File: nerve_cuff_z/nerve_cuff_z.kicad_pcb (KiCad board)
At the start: 2 copper layers, 4 x 5.7 mm, 4 parts

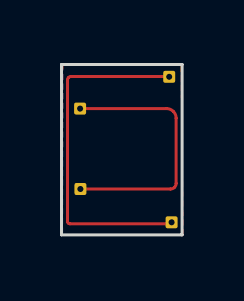
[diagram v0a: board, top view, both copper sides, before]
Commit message: fixing minor DRC problems for z cuff
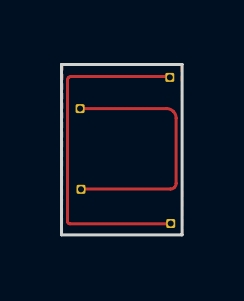
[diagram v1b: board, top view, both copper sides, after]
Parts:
- removed the REF** at (103.5, 65.3)
- removed the REF** at (100.6, 69.1)
- removed the REF** at (103.6, 70.2)
- added REF**: solder_wire_pad, nerve_cuff_pad:solder_wire_pad, F.Cu at (103.6, 70.2)
- added REF**: solder_wire_pad, nerve_cuff_pad:solder_wire_pad, F.Cu at (103.6, 65.3)
- added REF**: solder_wire_pad, nerve_cuff_pad:solder_wire_pad, F.Cu at (100.6, 69.1)
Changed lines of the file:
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@@
   (net 0 "")
   (footprint "nerve_cuff_pad:solder_wire_pad" (layer "F.Cu")
-    (at 103.55 65.33)
+    (at 103.6 70.22)
     (descr "Soldered wire connection, for a single 0.1 mm² wire, basic insulation, conductor diameter 0.4mm, outer diameter 1mm, size source Multi-Contact FLEXI-E 0.1 (https://ec.staubli.com/AcroFiles/Catalogues/TM_Cab-Main-11014119_(en)_hi.pdf), bend radius 3 times outer diameter, generated with kicad-footprint-generator")
     (tags "connector wire 0.1sqmm")
@@
     (fp_line (start 0.2 0.2) (end 0.2 -0.2)
       (stroke (width 0.05) (type solid)) (layer "F.CrtYd"))
-    (pad "1" thru_hole roundrect (at 0 0) (size 0.4 0.4) (drill 0.2) (layers "*.Cu" "*.Mask") (roundrect_rratio 0.15625))
+    (pad "1" thru_hole roundrect (at 0 0) (size 0.3 0.3) (drill 0.2) (layers "*.Cu" "*.Mask") (roundrect_rratio 0.15625))
     (model "${KICAD6_3DMODEL_DIR}/Connector_Wire.3dshapes/SolderWire-0.1sqmm_1x01_D0.4mm_OD1mm.wrl"
       (offset (xyz 0 0 0))
@@
   )
   (footprint "nerve_cuff_pad:solder_wire_pad" (layer "F.Cu")
-    (at 100.59 69.07)
+    (at 103.57 65.35)
     (descr "Soldered wire connection, for a single 0.1 mm² wire, basic insulation, conductor diameter 0.4mm, outer diameter 1mm, size source Multi-Contact FLEXI-E 0.1 (https://ec.staubli.com/AcroFiles/Catalogues/TM_Cab-Main-11014119_(en)_hi.pdf), bend radius 3 times outer diameter, generated with kicad-footprint-generator")
     (tags "connector wire 0.1sqmm")
@@
     (fp_line (start 0.2 0.2) (end 0.2 -0.2)
       (stroke (width 0.05) (type solid)) (layer "F.CrtYd"))
-    (pad "1" thru_hole roundrect (at 0 0) (size 0.4 0.4) (drill 0.2) (layers "*.Cu" "*.Mask") (roundrect_rratio 0.15625))
+    (pad "1" thru_hole roundrect (at 0 0) (size 0.3 0.3) (drill 0.2) (layers "*.Cu" "*.Mask") (roundrect_rratio 0.15625))
     (model "${KICAD6_3DMODEL_DIR}/Connector_Wire.3dshapes/SolderWire-0.1sqmm_1x01_D0.4mm_OD1mm.wrl"
       (offset (xyz 0 0 0))
@@
     (fp_line (start 0.2 0.2) (end 0.2 -0.2)
       (stroke (width 0.05) (type solid)) (layer "F.CrtYd"))
-    (pad "1" thru_hole roundrect (at 0 0) (size 0.4 0.4) (drill 0.2) (layers "*.Cu" "*.Mask") (roundrect_rratio 0.15625))
+    (pad "1" thru_hole roundrect (at 0 0) (size 0.3 0.3) (drill 0.2) (layers "*.Cu" "*.Mask") (roundrect_rratio 0.15625))
     (model "${KICAD6_3DMODEL_DIR}/Connector_Wire.3dshapes/SolderWire-0.1sqmm_1x01_D0.4mm_OD1mm.wrl"
       (offset (xyz 0 0 0))
@@
   )
   (footprint "nerve_cuff_pad:solder_wire_pad" (layer "F.Cu")
-    (at 103.63 70.18)
+    (at 100.61 69.08)
     (descr "Soldered wire connection, for a single 0.1 mm² wire, basic insulation, conductor diameter 0.4mm, outer diameter 1mm, size source Multi-Contact FLEXI-E 0.1 (https://ec.staubli.com/AcroFiles/Catalogues/TM_Cab-Main-11014119_(en)_hi.pdf), bend radius 3 times outer diameter, generated with kicad-footprint-generator")
     (tags "connector wire 0.1sqmm")
@@
     (fp_line (start 0.2 0.2) (end 0.2 -0.2)
       (stroke (width 0.05) (type solid)) (layer "F.CrtYd"))
-    (pad "1" thru_hole roundrect (at 0 0) (size 0.4 0.4) (drill 0.2) (layers "*.Cu" "*.Mask") (roundrect_rratio 0.15625))
+    (pad "1" thru_hole roundrect (at 0 0) (size 0.3 0.3) (drill 0.2) (layers "*.Cu" "*.Mask") (roundrect_rratio 0.15625))
     (model "${KICAD6_3DMODEL_DIR}/Connector_Wire.3dshapes/SolderWire-0.1sqmm_1x01_D0.4mm_OD1mm.wrl"
       (offset (xyz 0 0 0))
@@
   (segment (start 100.16 65.439497) (end 100.16 70.144644) (width 0.1) (layer "F.Cu") (net 0))
   (segment (start 103.54 65.32) (end 100.279497 65.32) (width 0.1) (layer "F.Cu") (net 0))
+  (segment (start 103.592218 69.07) (end 100.59 69.07) (width 0.1) (layer "F.Cu") (net 0))
   (segment (start 103.461706 66.39) (end 100.58 66.39) (width 0.1) (layer "F.Cu") (net 0))
-  (segment (start 103.592218 69.07) (end 100.59 69.07) (width 0.1) (layer "F.Cu") (net 0))
   (segment (start 103.58 70.23) (end 103.63 70.18) (width 0.1) (layer "F.Cu") (net 0))
   (arc (start 100.279497 65.32) (mid 100.233768 65.329096) (end 100.195 65.355) (width 0.1) (layer "F.Cu") (net 0))

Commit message: all boards cleaned up + passing DRC
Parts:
- moved REF** 0.07 mm to (103.5, 70.2)
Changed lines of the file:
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@@
   (net 0 "")
   (footprint "nerve_cuff_pad:solder_wire_pad" (layer "F.Cu")
-    (at 103.6 70.22)
+    (at 103.53 70.21)
     (descr "Soldered wire connection, for a single 0.1 mm² wire, basic insulation, conductor diameter 0.4mm, outer diameter 1mm, size source Multi-Contact FLEXI-E 0.1 (https://ec.staubli.com/AcroFiles/Catalogues/TM_Cab-Main-11014119_(en)_hi.pdf), bend radius 3 times outer diameter, generated with kicad-footprint-generator")
     (tags "connector wire 0.1sqmm")
@@
         (effects (font (size 1 1) (thickness 0.15)))
     )
-    (fp_line (start -0.2 -0.2) (end -0.2 0.2)
+    (fp_line (start -0.3 -0.3) (end -0.3 0.3)
       (stroke (width 0.05) (type solid)) (layer "F.CrtYd"))
-    (fp_line (start -0.2 0.2) (end 0.2 0.2)
+    (fp_line (start -0.3 0.3) (end 0.3 0.3)
       (stroke (width 0.05) (type solid)) (layer "F.CrtYd"))
-    (fp_line (start 0.2 -0.2) (end -0.2 -0.2)
+    (fp_line (start 0.3 -0.3) (end -0.3 -0.3)
       (stroke (width 0.05) (type solid)) (layer "F.CrtYd"))
-    (fp_line (start 0.2 0.2) (end 0.2 -0.2)
+    (fp_line (start 0.3 0.3) (end 0.3 -0.3)
       (stroke (width 0.05) (type solid)) (layer "F.CrtYd"))
     (pad "1" thru_hole roundrect (at 0 0) (size 0.3 0.3) (drill 0.2) (layers "*.Cu" "*.Mask") (roundrect_rratio 0.15625))
@@
         (effects (font (size 1 1) (thickness 0.15)))
     )
-    (fp_line (start -0.2 -0.2) (end -0.2 0.2)
+    (fp_line (start -0.3 -0.3) (end -0.3 0.3)
       (stroke (width 0.05) (type solid)) (layer "F.CrtYd"))
-    (fp_line (start -0.2 0.2) (end 0.2 0.2)
+    (fp_line (start -0.3 0.3) (end 0.3 0.3)
       (stroke (width 0.05) (type solid)) (layer "F.CrtYd"))
-    (fp_line (start 0.2 -0.2) (end -0.2 -0.2)
+    (fp_line (start 0.3 -0.3) (end -0.3 -0.3)
       (stroke (width 0.05) (type solid)) (layer "F.CrtYd"))
-    (fp_line (start 0.2 0.2) (end 0.2 -0.2)
+    (fp_line (start 0.3 0.3) (end 0.3 -0.3)
       (stroke (width 0.05) (type solid)) (layer "F.CrtYd"))
     (pad "1" thru_hole roundrect (at 0 0) (size 0.3 0.3) (drill 0.2) (layers "*.Cu" "*.Mask") (roundrect_rratio 0.15625))
@@
         (effects (font (size 1 1) (thickness 0.15)))
     )
-    (fp_line (start -0.2 -0.2) (end -0.2 0.2)
+    (fp_line (start -0.3 -0.3) (end -0.3 0.3)
       (stroke (width 0.05) (type solid)) (layer "F.CrtYd"))
-    (fp_line (start -0.2 0.2) (end 0.2 0.2)
+    (fp_line (start -0.3 0.3) (end 0.3 0.3)
       (stroke (width 0.05) (type solid)) (layer "F.CrtYd"))
-    (fp_line (start 0.2 -0.2) (end -0.2 -0.2)
+    (fp_line (start 0.3 -0.3) (end -0.3 -0.3)
       (stroke (width 0.05) (type solid)) (layer "F.CrtYd"))
-    (fp_line (start 0.2 0.2) (end 0.2 -0.2)
+    (fp_line (start 0.3 0.3) (end 0.3 -0.3)
       (stroke (width 0.05) (type solid)) (layer "F.CrtYd"))
     (pad "1" thru_hole roundrect (at 0 0) (size 0.3 0.3) (drill 0.2) (layers "*.Cu" "*.Mask") (roundrect_rratio 0.15625))
@@
         (effects (font (size 1 1) (thickness 0.15)))
     )
-    (fp_line (start -0.2 -0.2) (end -0.2 0.2)
+    (fp_line (start -0.3 -0.3) (end -0.3 0.3)
       (stroke (width 0.05) (type solid)) (layer "F.CrtYd"))
-    (fp_line (start -0.2 0.2) (end 0.2 0.2)
+    (fp_line (start -0.3 0.3) (end 0.3 0.3)
       (stroke (width 0.05) (type solid)) (layer "F.CrtYd"))
-    (fp_line (start 0.2 -0.2) (end -0.2 -0.2)
+    (fp_line (start 0.3 -0.3) (end -0.3 -0.3)
       (stroke (width 0.05) (type solid)) (layer "F.CrtYd"))
-    (fp_line (start 0.2 0.2) (end 0.2 -0.2)
+    (fp_line (start 0.3 0.3) (end 0.3 -0.3)
       (stroke (width 0.05) (type solid)) (layer "F.CrtYd"))
     (pad "1" thru_hole roundrect (at 0 0) (size 0.3 0.3) (drill 0.2) (layers "*.Cu" "*.Mask") (roundrect_rratio 0.15625))
@@
   )
   (dimension (type aligned) (layer "F.SilkS")
-    (pts (xy 103.98 64.92) (xy 103.98 70.6))
+    (pts (xy 103.3 65.29) (xy 103.3 70.97))
     (height -5.97)
-    (gr_text "5.6800 mm" (at 108.8 67.76 90) (layer "F.SilkS")
+    (gr_text "5.6800 mm" (at 108.12 68.13 90) (layer "F.SilkS")
       (effects (font (size 1 1) (thickness 0.15)))
     )
@@
     (style (thickness 0.15) (arrow_length 1.27) (text_position_mode 0) (extension_height 0.58642) (extension_offset 0.5) keep_text_aligned)
   )
-  (segment (start 100.245355 70.23) (end 103.58 70.23) (width 0.1) (layer "F.Cu") (net 0))
+  (segment (start 100.245355 70.23) (end 103.51 70.23) (width 0.1) (layer "F.Cu") (net 0))
   (segment (start 103.78 68.882218) (end 103.78 66.708293) (width 0.1) (layer "F.Cu") (net 0))
+  (segment (start 103.54 65.32) (end 100.279497 65.32) (width 0.1) (layer "F.Cu") (net 0))
   (segment (start 100.16 65.439497) (end 100.16 70.144644) (width 0.1) (layer "F.Cu") (net 0))
-  (segment (start 103.54 65.32) (end 100.279497 65.32) (width 0.1) (layer "F.Cu") (net 0))
   (segment (start 103.592218 69.07) (end 100.59 69.07) (width 0.1) (layer "F.Cu") (net 0))
   (segment (start 103.461706 66.39) (end 100.58 66.39) (width 0.1) (layer "F.Cu") (net 0))
-  (segment (start 103.58 70.23) (end 103.63 70.18) (width 0.1) (layer "F.Cu") (net 0))
-  (arc (start 100.279497 65.32) (mid 100.233768 65.329096) (end 100.195 65.355) (width 0.1) (layer "F.Cu") (net 0))
   (arc (start 103.78 68.882218) (mid 103.765705 68.954079) (end 103.725 69.015) (width 0.1) (layer "F.Cu") (net 0))
+  (arc (start 100.195 65.355) (mid 100.169096 65.393767) (end 100.16 65.439497) (width 0.1) (layer "F.Cu") (net 0))
+  (arc (start 100.185 70.205) (mid 100.212691 70.223508) (end 100.245355 70.23) (width 0.1) (layer "F.Cu") (net 0))
   (arc (start 103.686774 66.483226) (mid 103.583512 66.414228) (end 103.461706 66.39) (width 0.1) (layer "F.Cu") (net 0))
   (arc (start 103.725 69.015) (mid 103.664079 69.055705) (end 103.592218 69.07) (width 0.1) (layer "F.Cu") (net 0))
   (arc (start 103.686774 66.483226) (mid 103.755771 66.586487) (end 103.78 66.708293) (width 0.1) (layer "F.Cu") (net 0))
   (arc (start 100.16 70.144644) (mid 100.166497 70.177308) (end 100.185 70.205) (width 0.1) (layer "F.Cu") (net 0))
-  (arc (start 100.185 70.205) (mid 100.212691 70.223496) (end 100.245355 70.23) (width 0.1) (layer "F.Cu") (net 0))
-  (arc (start 100.195 65.355) (mid 100.169096 65.393767) (end 100.16 65.439497) (width 0.1) (layer "F.Cu") (net 0))
+  (arc (start 100.279497 65.32) (mid 100.233768 65.329096) (end 100.195 65.355) (width 0.1) (layer "F.Cu") (net 0))
   (zone (net 0) (net_name "") (layer "F.Cu") (hatch edge 0.1)
     (connect_pads (clearance 0.05))

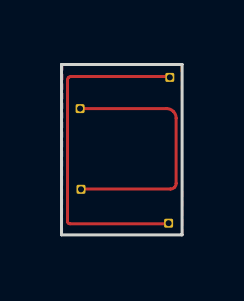
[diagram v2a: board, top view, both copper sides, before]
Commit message: updating clearances for xy gradient board
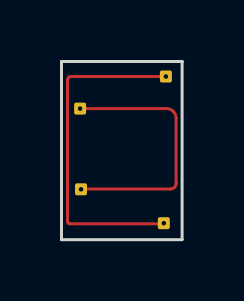
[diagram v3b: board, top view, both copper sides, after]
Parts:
- moved REF** 0.16 mm to (103.4, 70.2)
- moved REF** 0.13 mm to (103.4, 65.3)
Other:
- board size 4 x 5.7 mm -> 4 x 5.9 mm
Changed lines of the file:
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@@
   (net 0 "")
   (footprint "nerve_cuff_pad:solder_wire_pad" (layer "F.Cu")
-    (at 103.53 70.21)
+    (at 103.37 70.21)
     (descr "Soldered wire connection, for a single 0.1 mm² wire, basic insulation, conductor diameter 0.4mm, outer diameter 1mm, size source Multi-Contact FLEXI-E 0.1 (https://ec.staubli.com/AcroFiles/Catalogues/TM_Cab-Main-11014119_(en)_hi.pdf), bend radius 3 times outer diameter, generated with kicad-footprint-generator")
     (tags "connector wire 0.1sqmm")
@@
     (fp_line (start 0.3 0.3) (end 0.3 -0.3)
       (stroke (width 0.05) (type solid)) (layer "F.CrtYd"))
-    (pad "1" thru_hole roundrect (at 0 0) (size 0.3 0.3) (drill 0.2) (layers "*.Cu" "*.Mask") (roundrect_rratio 0.15625))
+    (pad "1" thru_hole roundrect (at 0 0) (size 0.4 0.4) (drill 0.15) (layers "*.Cu" "*.Mask") (roundrect_rratio 0.15625))
     (model "${KICAD6_3DMODEL_DIR}/Connector_Wire.3dshapes/SolderWire-0.1sqmm_1x01_D0.4mm_OD1mm.wrl"
       (offset (xyz 0 0 0))
@@
   )
   (footprint "nerve_cuff_pad:solder_wire_pad" (layer "F.Cu")
-    (at 103.57 65.35)
+    (at 103.44 65.32)
     (descr "Soldered wire connection, for a single 0.1 mm² wire, basic insulation, conductor diameter 0.4mm, outer diameter 1mm, size source Multi-Contact FLEXI-E 0.1 (https://ec.staubli.com/AcroFiles/Catalogues/TM_Cab-Main-11014119_(en)_hi.pdf), bend radius 3 times outer diameter, generated with kicad-footprint-generator")
     (tags "connector wire 0.1sqmm")
@@
     (fp_line (start 0.3 0.3) (end 0.3 -0.3)
       (stroke (width 0.05) (type solid)) (layer "F.CrtYd"))
-    (pad "1" thru_hole roundrect (at 0 0) (size 0.3 0.3) (drill 0.2) (layers "*.Cu" "*.Mask") (roundrect_rratio 0.15625))
+    (pad "1" thru_hole roundrect (at 0 0) (size 0.4 0.4) (drill 0.15) (layers "*.Cu" "*.Mask") (roundrect_rratio 0.15625))
     (model "${KICAD6_3DMODEL_DIR}/Connector_Wire.3dshapes/SolderWire-0.1sqmm_1x01_D0.4mm_OD1mm.wrl"
       (offset (xyz 0 0 0))
@@
     (fp_line (start 0.3 0.3) (end 0.3 -0.3)
       (stroke (width 0.05) (type solid)) (layer "F.CrtYd"))
-    (pad "1" thru_hole roundrect (at 0 0) (size 0.3 0.3) (drill 0.2) (layers "*.Cu" "*.Mask") (roundrect_rratio 0.15625))
+    (pad "1" thru_hole roundrect (at 0 0) (size 0.4 0.4) (drill 0.15) (layers "*.Cu" "*.Mask") (roundrect_rratio 0.15625))
     (model "${KICAD6_3DMODEL_DIR}/Connector_Wire.3dshapes/SolderWire-0.1sqmm_1x01_D0.4mm_OD1mm.wrl"
       (offset (xyz 0 0 0))
@@
     (fp_line (start 0.3 0.3) (end 0.3 -0.3)
       (stroke (width 0.05) (type solid)) (layer "F.CrtYd"))
-    (pad "1" thru_hole roundrect (at 0 0) (size 0.3 0.3) (drill 0.2) (layers "*.Cu" "*.Mask") (roundrect_rratio 0.15625))
+    (pad "1" thru_hole roundrect (at 0 0) (size 0.4 0.4) (drill 0.15) (layers "*.Cu" "*.Mask") (roundrect_rratio 0.15625))
     (model "${KICAD6_3DMODEL_DIR}/Connector_Wire.3dshapes/SolderWire-0.1sqmm_1x01_D0.4mm_OD1mm.wrl"
       (offset (xyz 0 0 0))
@@
     )
   )
-  (gr_line (start 103.98 70.6) (end 103.98 64.92)
+  (gr_line (start 103.98 70.76) (end 103.98 64.82)
     (stroke (width 0.1) (type default)) (layer "Edge.Cuts"))
-  (gr_line (start 103.98 64.92) (end 99.96 64.92)
+  (gr_line (start 103.98 64.82) (end 99.96 64.82)
     (stroke (width 0.1) (type default)) (layer "Edge.Cuts"))
-  (gr_line (start 99.96 64.92) (end 99.96 70.6)
+  (gr_line (start 99.96 64.82) (end 99.96 70.76)
     (stroke (width 0.1) (type default)) (layer "Edge.Cuts"))
-  (gr_line (start 99.96 70.6) (end 103.98 70.6)
+  (gr_line (start 99.96 70.76) (end 103.98 70.76)
     (stroke (width 0.1) (type default)) (layer "Edge.Cuts"))
   (dimension (type aligned) (layer "F.SilkS")
@@
     (style (thickness 0.15) (arrow_length 1.27) (text_position_mode 0) (extension_height 0.58642) (extension_offset 0.5) keep_text_aligned)
   )
-  (dimension (type aligned) (layer "F.SilkS")
-    (pts (xy 103.3 65.29) (xy 103.3 70.97))
-    (height -5.97)
-    (gr_text "5.6800 mm" (at 108.12 68.13 90) (layer "F.SilkS")
+  (dimension (type aligned) (layer "Edge.Cuts")
+    (pts (xy 103.97 64.83) (xy 103.98 70.77))
+    (height -3.197611)
+    (gr_text "5.9400 mm" (at 108.322604 67.792681 270.0964575) (layer "Edge.Cuts")
       (effects (font (size 1 1) (thickness 0.15)))
     )
     (format (prefix "") (suffix "") (units 3) (units_format 1) (precision 4))
-    (style (thickness 0.15) (arrow_length 1.27) (text_position_mode 0) (extension_height 0.58642) (extension_offset 0.5) keep_text_aligned)
+    (style (thickness 0.1) (arrow_length 1.27) (text_position_mode 0) (extension_height 0.58642) (extension_offset 0.5) keep_text_aligned)
   )
   (segment (start 100.245355 70.23) (end 103.51 70.23) (width 0.1) (layer "F.Cu") (net 0))
+  (segment (start 100.256529 65.32) (end 100.255861 65.320668) (width 0.1) (layer "F.Cu") (net 0))
   (segment (start 103.78 68.882218) (end 103.78 66.708293) (width 0.1) (layer "F.Cu") (net 0))
-  (segment (start 103.54 65.32) (end 100.279497 65.32) (width 0.1) (layer "F.Cu") (net 0))
+  (segment (start 103.121336 65.32) (end 100.256529 65.32) (width 0.1) (layer "F.Cu") (net 0))
   (segment (start 100.16 65.439497) (end 100.16 70.144644) (width 0.1) (layer "F.Cu") (net 0))
   (segment (start 103.592218 69.07) (end 100.59 69.07) (width 0.1) (layer "F.Cu") (net 0))
+  (segment (start 103.121336 65.32) (end 103.44 65.32) (width 0.1) (layer "F.Cu") (net 0))
+  (segment (start 103.120668 65.320668) (end 103.121336 65.32) (width 0.1) (layer "F.Cu") (net 0))
   (segment (start 103.461706 66.39) (end 100.58 66.39) (width 0.1) (layer "F.Cu") (net 0))
   (arc (start 103.78 68.882218) (mid 103.765705 68.954079) (end 103.725 69.015) (width 0.1) (layer "F.Cu") (net 0))
+  (arc (start 103.686774 66.483226) (mid 103.583512 66.414228) (end 103.461706 66.39) (width 0.1) (layer "F.Cu") (net 0))
   (arc (start 100.195 65.355) (mid 100.169096 65.393767) (end 100.16 65.439497) (width 0.1) (layer "F.Cu") (net 0))
+  (arc (start 103.725 69.015) (mid 103.664079 69.055705) (end 103.592218 69.07) (width 0.1) (layer "F.Cu") (net 0))
+  (arc (start 100.16 70.144644) (mid 100.166497 70.177308) (end 100.185 70.205) (width 0.1) (layer "F.Cu") (net 0))
+  (arc (start 103.686774 66.483226) (mid 103.755771 66.586487) (end 103.78 66.708293) (width 0.1) (layer "F.Cu") (net 0))
   (arc (start 100.185 70.205) (mid 100.212691 70.223508) (end 100.245355 70.23) (width 0.1) (layer "F.Cu") (net 0))
-  (arc (start 103.686774 66.483226) (mid 103.583512 66.414228) (end 103.461706 66.39) (width 0.1) (layer "F.Cu") (net 0))
-  (arc (start 103.725 69.015) (mid 103.664079 69.055705) (end 103.592218 69.07) (width 0.1) (layer "F.Cu") (net 0))
-  (arc (start 103.686774 66.483226) (mid 103.755771 66.586487) (end 103.78 66.708293) (width 0.1) (layer "F.Cu") (net 0))
-  (arc (start 100.16 70.144644) (mid 100.166497 70.177308) (end 100.185 70.205) (width 0.1) (layer "F.Cu") (net 0))
-  (arc (start 100.279497 65.32) (mid 100.233768 65.329096) (end 100.195 65.355) (width 0.1) (layer "F.Cu") (net 0))
+  (arc (start 100.255861 65.320668) (mid 100.223167 65.33411) (end 100.195 65.355) (width 0.1) (layer "F.Cu") (net 0))
   (zone (net 0) (net_name "") (layer "F.Cu") (hatch edge 0.1)
     (connect_pads (clearance 0.05))
     (min_thickness 0.05) (filled_areas_thickness no)
-    (fill yes (thermal_gap 0.05) (thermal_bridge_width 0.05) (island_removal_mode 1) (island_area_min 10))
+    (fill (thermal_gap 0.05) (thermal_bridge_width 0.05) (island_removal_mode 1) (island_area_min 10))
     (polygon
       (pts
-        (xy 100 64.91)
-        (xy 99.98 70.61)
-        (xy 104.01 70.61)
-        (xy 103.95 64.92)
+        (xy 99.97 64.81)
+        (xy 99.97 70.77)
+        (xy 103.98 70.77)
+        (xy 103.97 64.83)
       )
     )
@@
     (connect_pads (clearance 0.05))
     (min_thickness 0.05) (filled_areas_thickness no)
-    (fill yes (thermal_gap 0.05) (thermal_bridge_width 0.05) (island_removal_mode 1) (island_area_min 10))
+    (fill (thermal_gap 0.05) (thermal_bridge_width 0.05) (island_removal_mode 1) (island_area_min 10))
     (polygon
       (pts
-        (xy 99.99 70.59)
-        (xy 103.99 70.6)
-        (xy 103.99 64.92)
-        (xy 100 64.92)
+        (xy 99.97 70.76)
+        (xy 103.98 70.76)
+        (xy 103.98 64.81)
+        (xy 99.96 64.82)
       )
     )
